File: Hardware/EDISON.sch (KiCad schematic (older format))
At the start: 5 parts, among them P5 CONN_01X06, SW2 PWR_BTN, U18 EdisonConnector

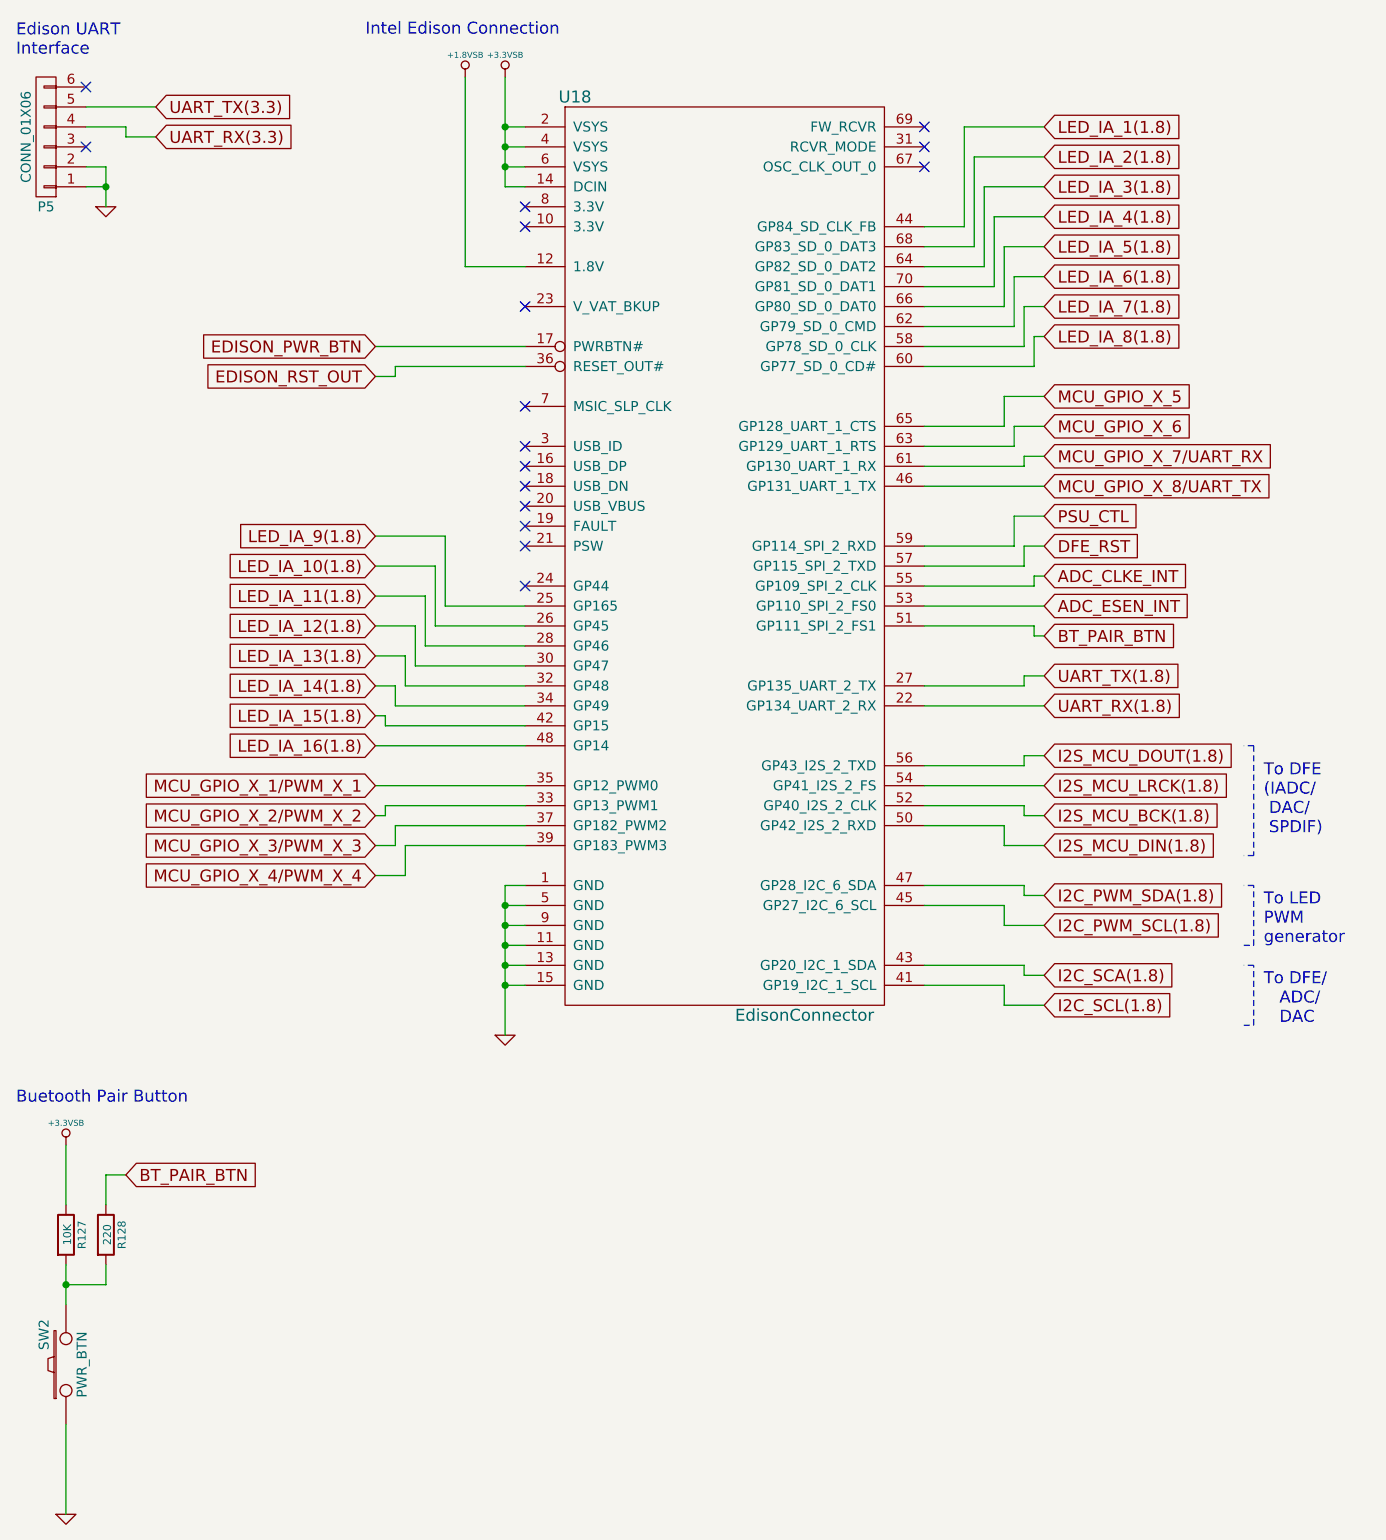
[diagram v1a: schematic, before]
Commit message: Updated Edison pins for 3.5mm connections
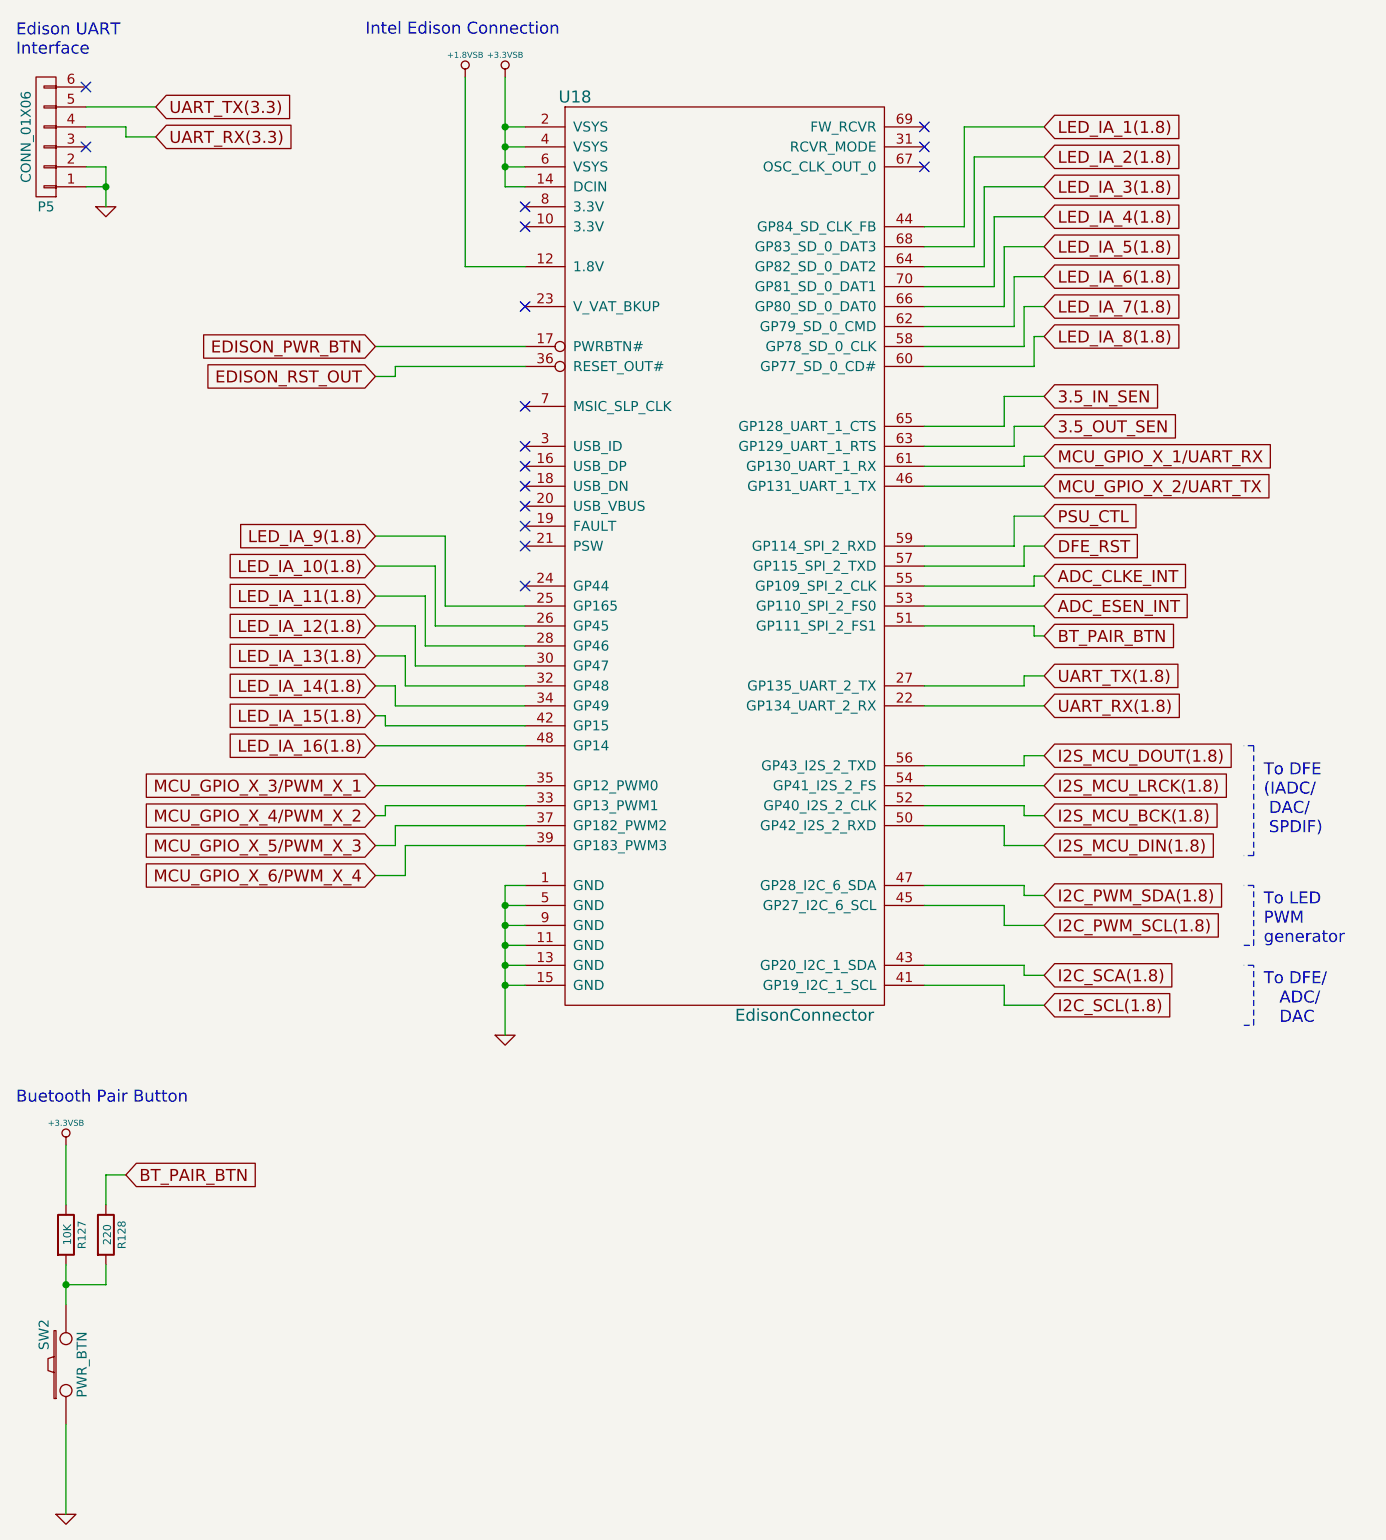
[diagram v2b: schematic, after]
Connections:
- net MCU_GPIO_X_1/PWM_X_1 renamed MCU_GPIO_X_3/PWM_X_1
- net MCU_GPIO_X_2/PWM_X_2 renamed MCU_GPIO_X_4/PWM_X_2
- net MCU_GPIO_X_3/PWM_X_3 renamed MCU_GPIO_X_5/PWM_X_3
- net MCU_GPIO_X_4/PWM_X_4 renamed MCU_GPIO_X_6/PWM_X_4
- net MCU_GPIO_X_5 renamed 3.5_IN_SEN
- net MCU_GPIO_X_6 renamed 3.5_OUT_SEN
- net MCU_GPIO_X_7/UART_RX renamed MCU_GPIO_X_1/UART_RX
- net MCU_GPIO_X_8/UART_TX renamed MCU_GPIO_X_2/UART_TX
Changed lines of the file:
@@
 Wire Wire Line
 	5850 5950 5450 5950
-Text GLabel 6050 3000 2    60   Input ~ 0
-MCU_GPIO_X_5
-Text GLabel 6050 3150 2    60   Input ~ 0
-MCU_GPIO_X_6
 Text GLabel 6050 3300 2    60   Input ~ 0
-MCU_GPIO_X_7/UART_RX
+MCU_GPIO_X_1/UART_RX
 Text GLabel 6050 3450 2    60   Input ~ 0
-MCU_GPIO_X_8/UART_TX
+MCU_GPIO_X_2/UART_TX
 Text GLabel 6050 3600 2    60   Input ~ 0
 PSU_CTL
@@
 	3050 3700 2700 3700
 Text GLabel 2700 4950 0    60   Input ~ 0
-MCU_GPIO_X_1/PWM_X_1
+MCU_GPIO_X_3/PWM_X_1
 Wire Wire Line
 	2700 4950 3450 4950
 Text GLabel 2700 5100 0    60   Input ~ 0
-MCU_GPIO_X_2/PWM_X_2
+MCU_GPIO_X_4/PWM_X_2
 Text GLabel 2700 5250 0    60   Input ~ 0
-MCU_GPIO_X_3/PWM_X_3
+MCU_GPIO_X_5/PWM_X_3
 Text GLabel 2700 5400 0    60   Input ~ 0
-MCU_GPIO_X_4/PWM_X_4
+MCU_GPIO_X_6/PWM_X_4
 Wire Wire Line
 	2700 5100 2750 5100
@@
 Buetooth Pair Button
 NoConn ~ 3450 3950
+Text GLabel 6050 3000 2    60   Input ~ 0
+3.5_IN_SEN
+Text GLabel 6050 3150 2    60   Input ~ 0
+3.5_OUT_SEN
 $EndSCHEMATC

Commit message: Updated libraries and place components into board layout
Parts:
- U18: footprint (none) -> muse-v2-lib:HIROSE_DF40C(2.0)-70DS-0.4V
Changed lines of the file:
@@
 F 0 "U18" H 3700 1600 60  0000 C CNN
 F 1 "EdisonConnector" H 4850 -3000 60  0000 C CNN
-F 2 "" H 3650 1950 60  0001 C CNN
+F 2 "muse-v2-lib:HIROSE_DF40C(2.0)-70DS-0.4V" H 3650 1950 60  0001 C CNN
 F 3 "" H 3650 1950 60  0000 C CNN
 	1    3650 1550

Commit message: Updated small schematic changes
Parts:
- U18: footprint muse-v2-lib:HIROSE_DF40C(2.0)-70DS-0.4V -> muse-v2-lib:Intel_Edison
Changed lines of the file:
@@
 F 0 "U18" H 3700 1600 60  0000 C CNN
 F 1 "EdisonConnector" H 4850 -3000 60  0000 C CNN
-F 2 "muse-v2-lib:HIROSE_DF40C(2.0)-70DS-0.4V" H 3650 1950 60  0001 C CNN
+F 2 "muse-v2-lib:Intel_Edison" H 3650 1950 60  0001 C CNN
 F 3 "" H 3650 1950 60  0000 C CNN
 	1    3650 1550
